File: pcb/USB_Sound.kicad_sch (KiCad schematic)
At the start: 36 parts, among them IC1 PCM2706, J1 USB4500-03-0-A_REVA, J2 Conn_Coaxial_x2, U5 FSUSB42MUX, U6 24AA02-OT, Y1 12Mhz

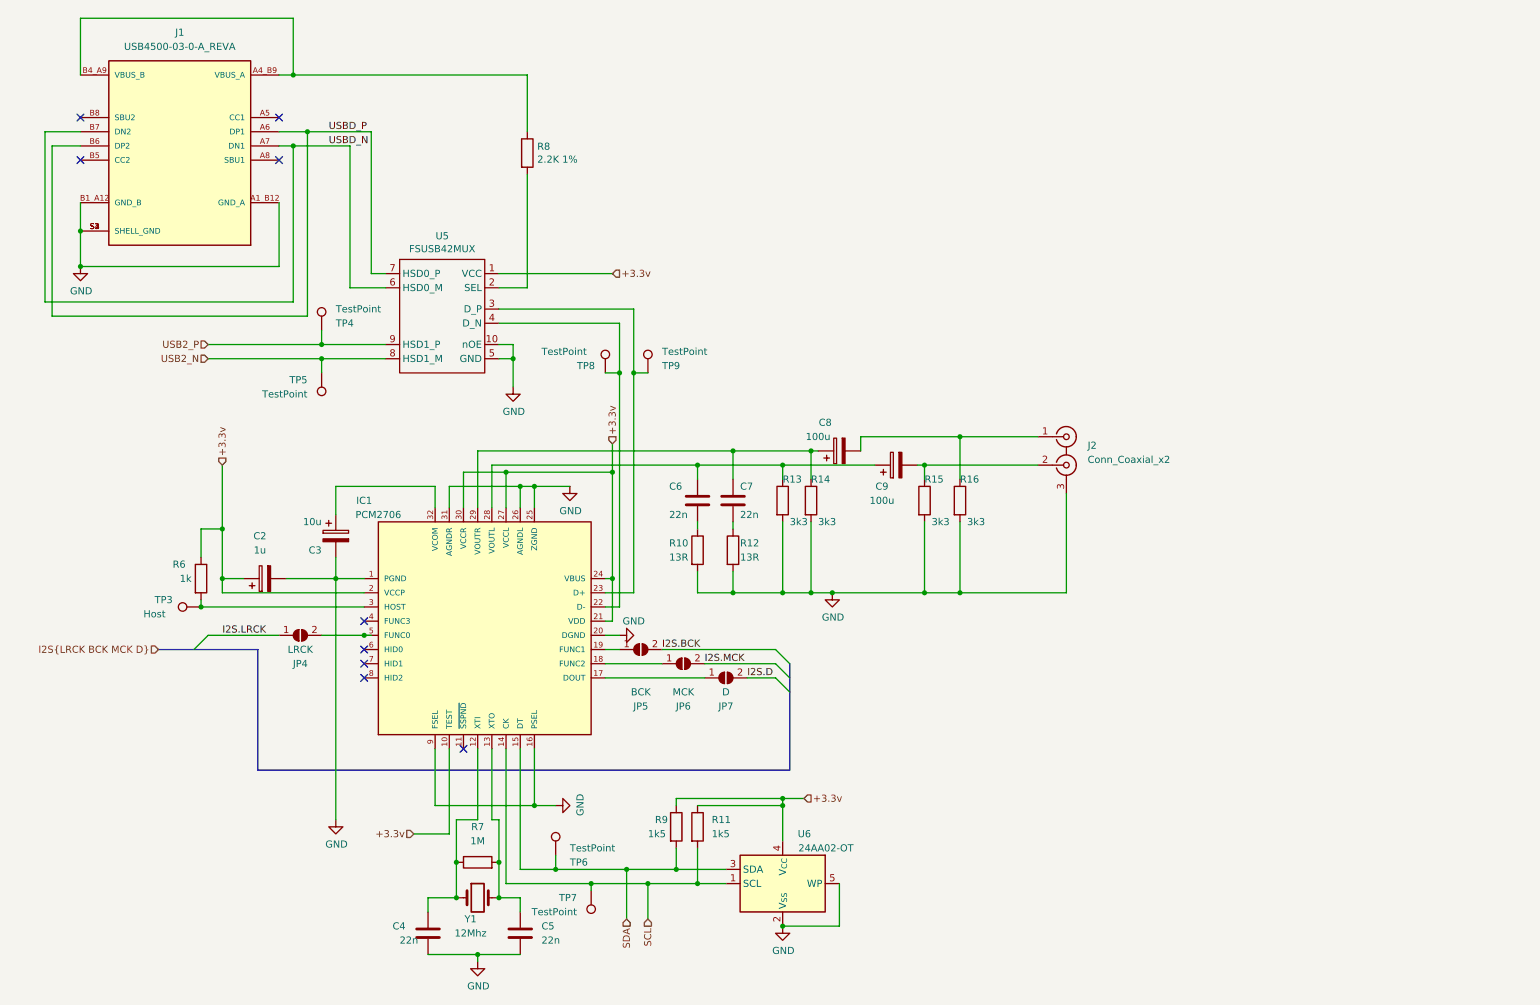
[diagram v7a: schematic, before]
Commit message: - work in progress, changed rj45 connector
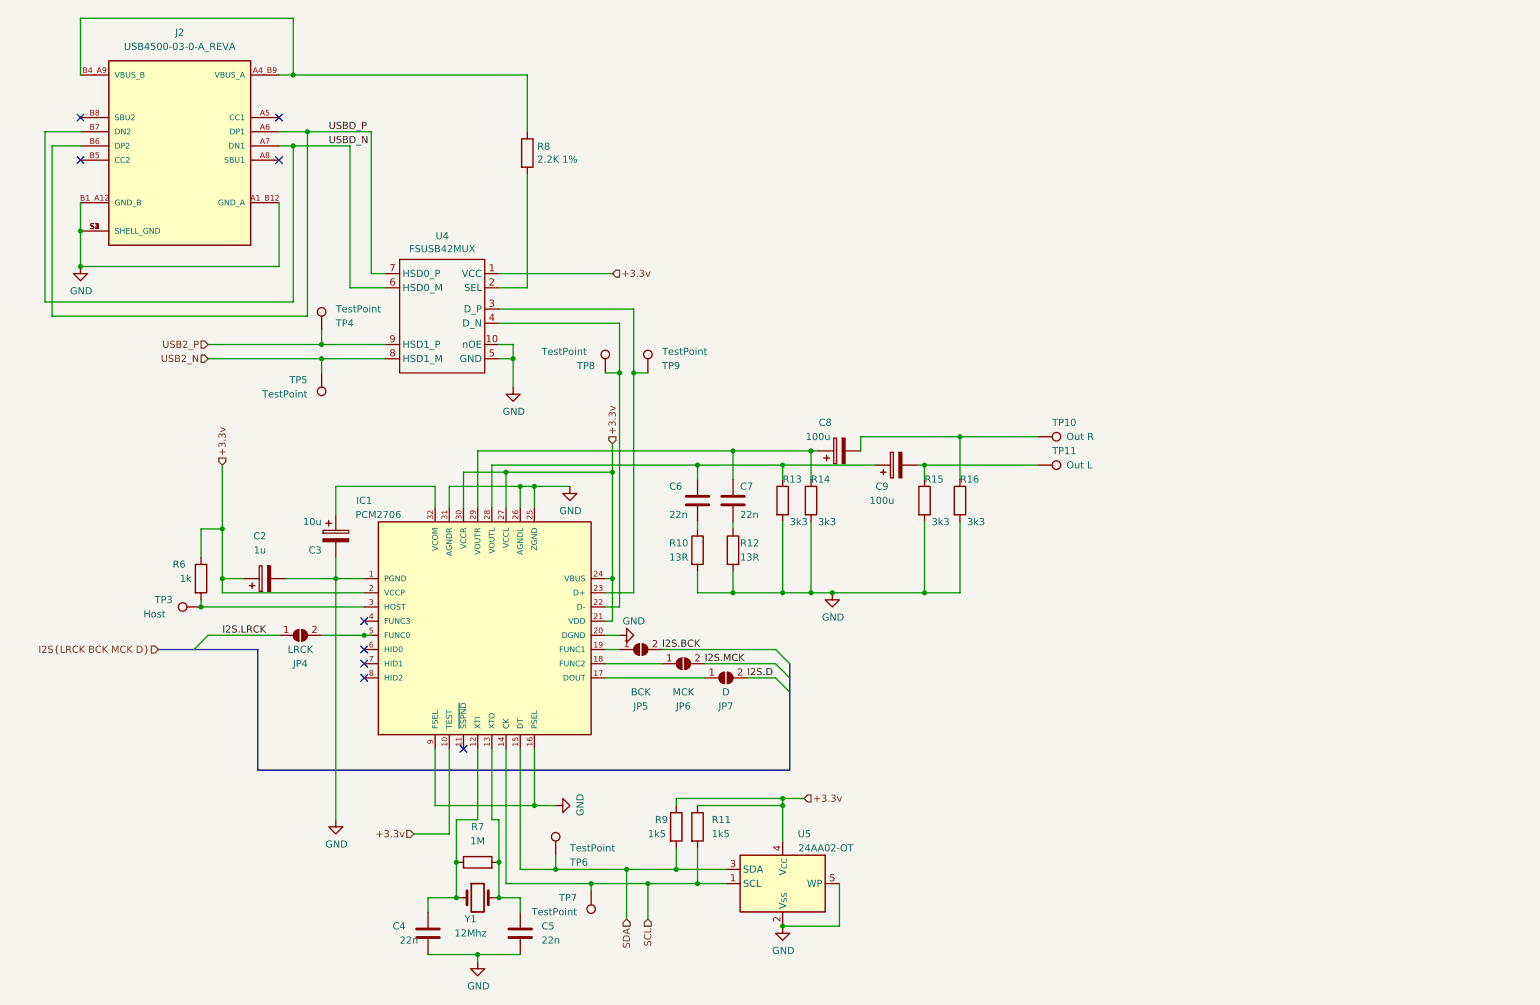
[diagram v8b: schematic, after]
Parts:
- removed J2: Conn_Coaxial_x2, symbol Connector:Conn_Coaxial_x2
- added TP10: Out R, TestPoint:TestPoint_Bridge_Pitch2.54mm_Drill1.0mm, symbol Connector:TestPoint
- added TP11: Out L, TestPoint:TestPoint_Bridge_Pitch2.54mm_Drill1.0mm, symbol Connector:TestPoint
- renumbered J1 to J2, U5 to U4, U6 to U5
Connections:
- net at C9.2, R15.1: now also TP11.1
- net at C8.2, R16.1: now also TP10.1
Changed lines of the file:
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@@
   (junction (at 151.13 163.83) (diameter 0) (color 0 0 0 0)
-  )
-  (junction (at 182.88 125.73) (diameter 0) (color 0 0 0 0)
   )
   (junction (at 151.13 162.56) (diameter 0) (color 0 0 0 0)
@@
     (stroke (width 0) (type default))
   )
-  (wire (pts (xy 201.93 125.73) (xy 182.88 125.73))
-    (stroke (width 0) (type default))
-  )
   (wire (pts (xy 106.68 153.67) (xy 106.68 163.83))
     (stroke (width 0) (type default))
@@
   )
   (wire (pts (xy 73.66 45.72) (xy 73.66 71.12))
-    (stroke (width 0) (type default))
-  )
-  (wire (pts (xy 201.93 107.95) (xy 201.93 125.73))
     (stroke (width 0) (type default))
   )
@@
   (symbol (lib_id "Memory_EEPROM:24AA02-OT") (at 151.13 177.8 0) (mirror y) (unit 1)
     (in_bom yes) (on_board yes) (dnp no)
-    (property "Reference" "U6" (at 156.21 168.91 0)
+    (property "Reference" "U5" (at 156.21 168.91 0)
       (effects (font (size 1.27 1.27)) (justify left))
     )
@@
       (project "VolumioAmp"
         (path "/c639bae0-d26f-43ee-9e8c-ca060284bd0b/93301fd2-7a6d-48be-bd24-243a1877e343"
-          (reference "U6") (unit 1)
+          (reference "U5") (unit 1)
         )
       )
@@
   (symbol (lib_id "USB4500-03-0-A_REVA:USB4500-03-0-A_REVA") (at 43.18 45.72 0) (mirror y) (unit 1)
     (in_bom yes) (on_board yes) (dnp no)
-    (property "Reference" "J1" (at 43.18 25.4 0)
+    (property "Reference" "J2" (at 43.18 25.4 0)
       (effects (font (size 1.27 1.27)))
     )
@@
       (project "VolumioAmp"
         (path "/c639bae0-d26f-43ee-9e8c-ca060284bd0b/93301fd2-7a6d-48be-bd24-243a1877e343"
-          (reference "J1") (unit 1)
+          (reference "J2") (unit 1)
         )
       )
@@
   (symbol (lib_id "CM4IO:FSUSB42MX") (at 91.44 85.09 0) (unit 1)
     (in_bom yes) (on_board yes) (dnp no)
-    (property "Reference" "U5" (at 90.17 61.849 0)
+    (property "Reference" "U4" (at 90.17 61.849 0)
       (effects (font (size 1.27 1.27)))
     )
@@
       (project "VolumioAmp"
         (path "/c639bae0-d26f-43ee-9e8c-ca060284bd0b/93301fd2-7a6d-48be-bd24-243a1877e343"
-          (reference "U5") (unit 1)
+          (reference "U4") (unit 1)
         )
       )
@@
     )
   )
+  (symbol (lib_id "Connector:TestPoint") (at 196.85 97.79 270) (unit 1)
+    (in_bom yes) (on_board yes) (dnp no)
+    (property "Reference" "TP10" (at 199.39 95.25 90)
+      (effects (font (size 1.27 1.27)) (justify left))
+    )
+    (property "Value" "Out R" (at 201.93 97.79 90)
+      (effects (font (size 1.27 1.27)) (justify left))
+    )
+    (property "Footprint" "TestPoint:TestPoint_Bridge_Pitch2.54mm_Drill1.0mm" (at 196.85 102.87 0)
+      (effects (font (size 1.27 1.27)) hide)
+    )
+    (property "Datasheet" "~" (at 196.85 102.87 0)
+      (effects (font (size 1.27 1.27)) hide)
+    )
+    (pin "1")
+    (instances
+      (project "VolumioAmp"
+        (path "/c639bae0-d26f-43ee-9e8c-ca060284bd0b/93301fd2-7a6d-48be-bd24-243a1877e343"
+          (reference "TP10") (unit 1)
+        )
+      )
+    )
+  )
   (symbol (lib_id "Device:R") (at 142.24 118.11 0) (unit 1)
     (in_bom yes) (on_board yes) (dnp no)
@@
     )
   )
-  (symbol (lib_id "Connector:Conn_Coaxial_x2") (at 201.93 100.33 0) (unit 1)
-    (in_bom yes) (on_board yes) (dnp no) (fields_autoplaced)
-    (property "Reference" "J2" (at 205.74 99.3532 0)
-      (effects (font (size 1.27 1.27)) (justify left))
-    )
-    (property "Value" "Conn_Coaxial_x2" (at 205.74 101.8932 0)
-      (effects (font (size 1.27 1.27)) (justify left))
-    )
-    (property "Footprint" "" (at 201.93 102.87 0)
-      (effects (font (size 1.27 1.27)) hide)
-    )
-    (property "Datasheet" " ~" (at 201.93 102.87 0)
-      (effects (font (size 1.27 1.27)) hide)
-    )
-    (pin "2")
-    (pin "3")
-    (pin "1")
-    (instances
-      (project "VolumioAmp"
-        (path "/c639bae0-d26f-43ee-9e8c-ca060284bd0b/93301fd2-7a6d-48be-bd24-243a1877e343"
-          (reference "J2") (unit 1)
-        )
-      )
-    )
-  )
   (symbol (lib_id "power:GND") (at 113.03 106.68 0) (unit 1)
     (in_bom yes) (on_board yes) (dnp no)
@@
         )
       )
+    )
+  )
+  (symbol (lib_id "Connector:TestPoint") (at 196.85 102.87 270) (unit 1)
+    (in_bom yes) (on_board yes) (dnp no)
+    (property "Reference" "TP11" (at 199.39 100.33 90)
+      (effects (font (size 1.27 1.27)) (justify left))
+    )
+    (property "Value" "Out L" (at 201.93 102.87 90)
+      (effects (font (size 1.27 1.27)) (justify left))
+    )
+    (property "Footprint" "TestPoint:TestPoint_Bridge_Pitch2.54mm_Drill1.0mm" (at 196.85 107.95 0)
+      (effects (font (size 1.27 1.27)) hide)
+    )
+    (property "Datasheet" "~" (at 196.85 107.95 0)
+      (effects (font (size 1.27 1.27)) hide)
+    )
+    (pin "1")
+    (instances
+      (project "VolumioAmp"
+        (path "/c639bae0-d26f-43ee-9e8c-ca060284bd0b/93301fd2-7a6d-48be-bd24-243a1877e343"
+          (reference "TP11") (unit 1)
+        )
+      )
